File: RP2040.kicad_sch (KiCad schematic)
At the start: 28 parts, among them J3 USB_C_Receptacle_USB2.0_16P, U1 RP2040, U2 AMS1117-3.3, U4 W25Q16JVSS, Y1 X322512MSB4SI

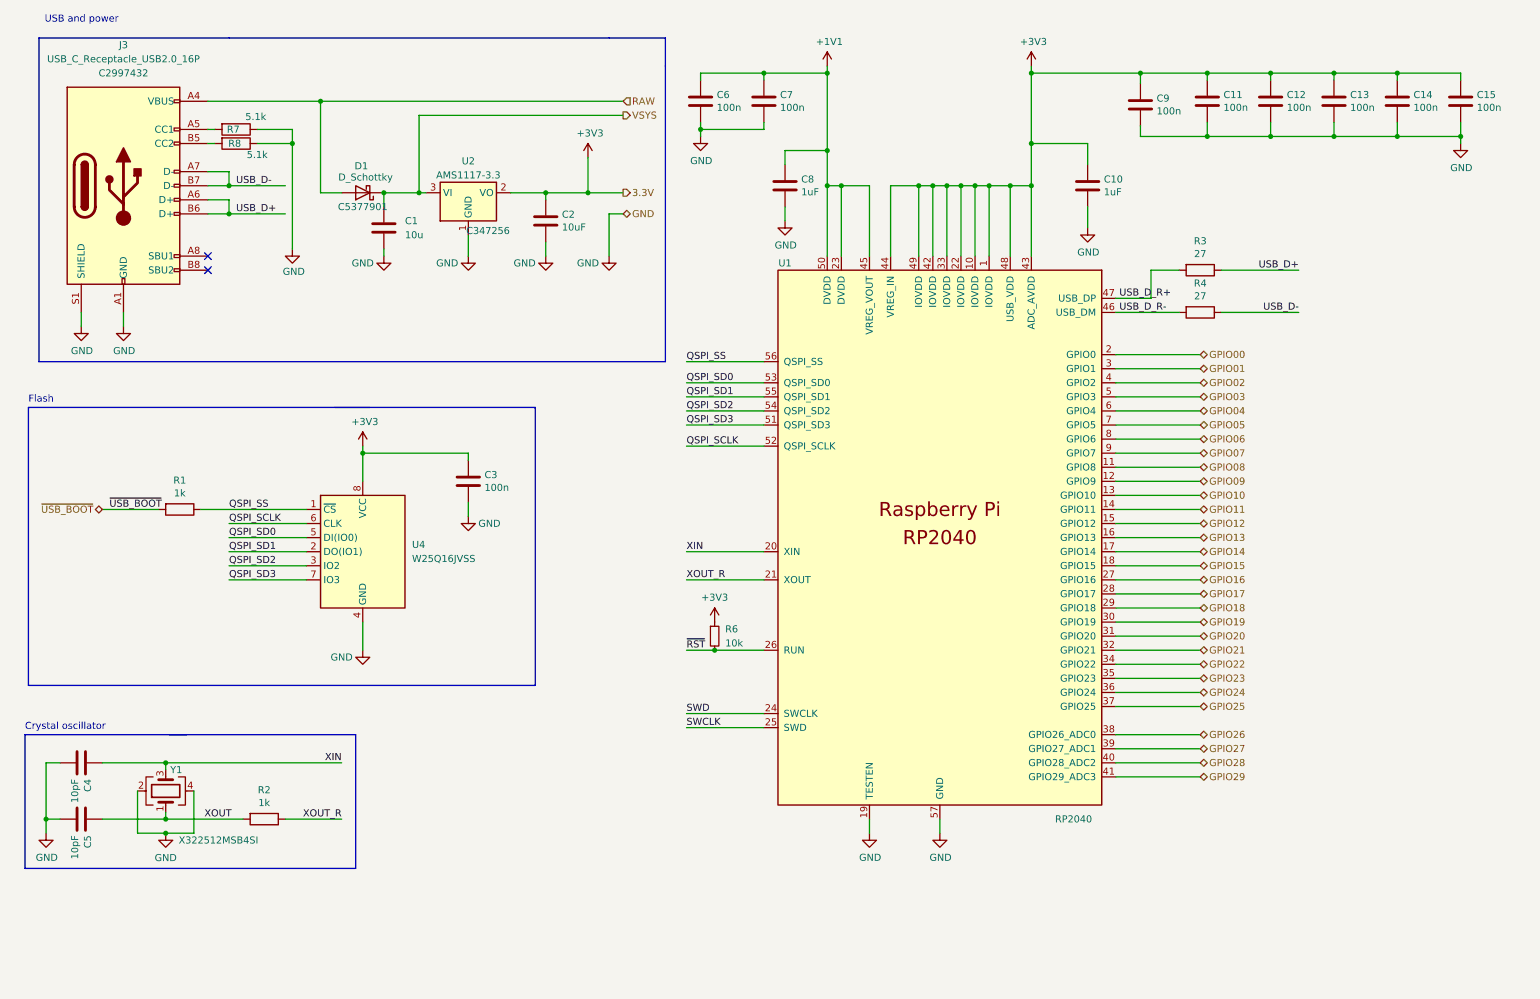
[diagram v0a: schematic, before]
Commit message: first changes for RP2350A
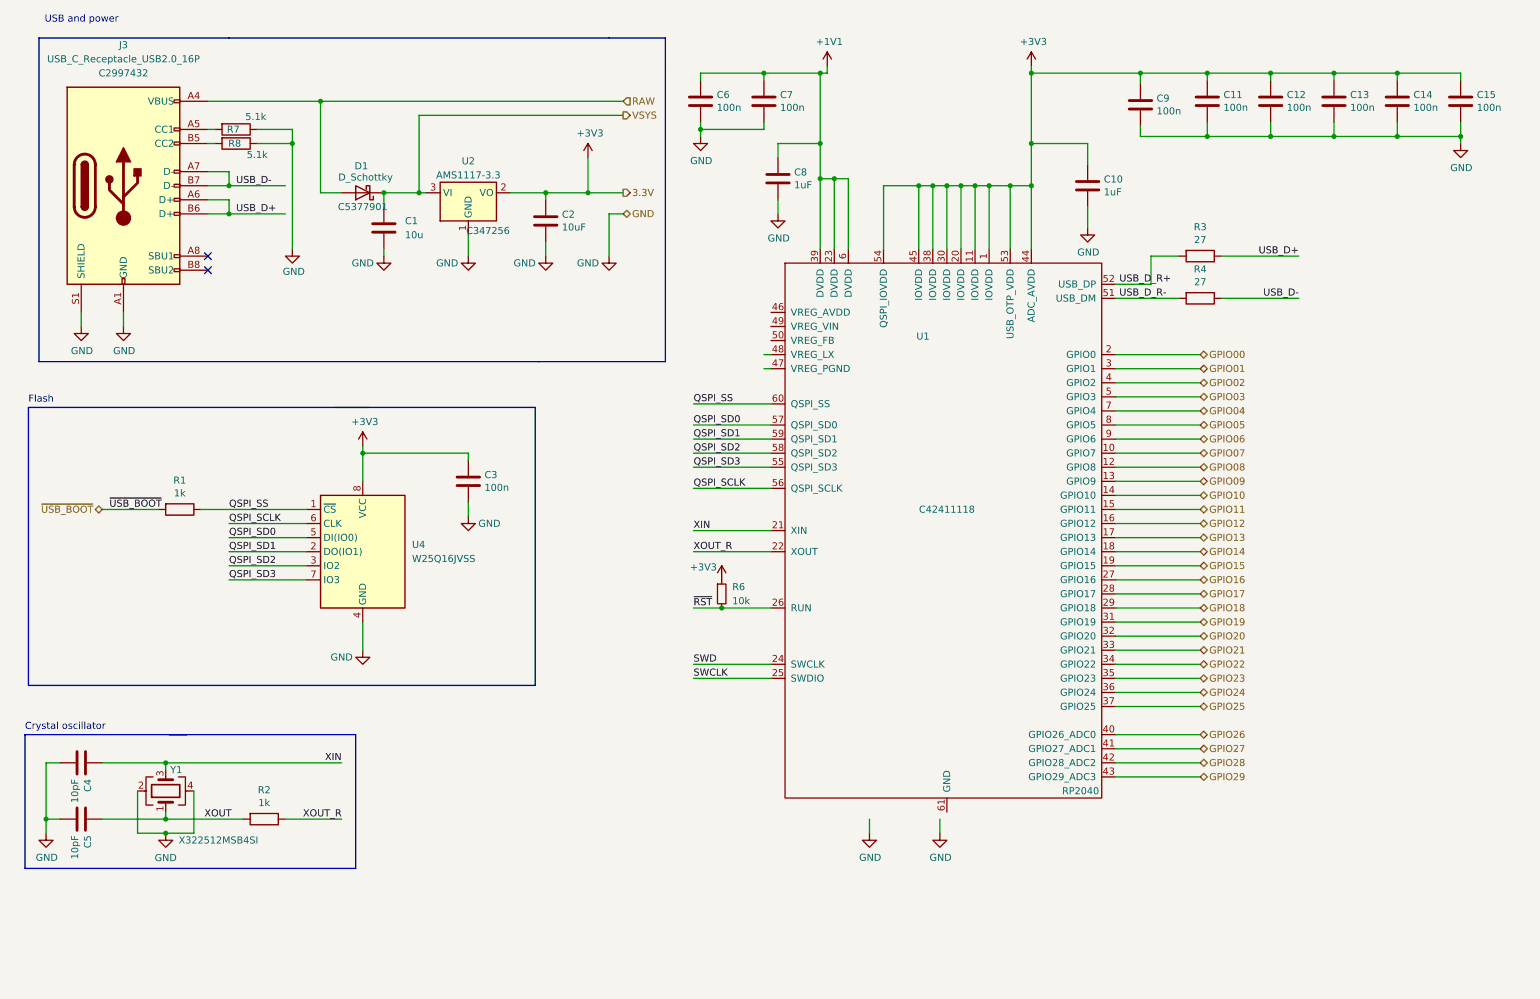
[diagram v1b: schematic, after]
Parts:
- U1: footprint _Neil:QFN56P40_700X700X90L40X18T310N -> _Own_Library:RP2350A_QFN-60_EP_7.75x7.75_Pitch0.4mm; symbol Custom_Symbols:RP2040 -> Own_Library:RP2350A-QFN60; JLCPCB (none) -> C42411118
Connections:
- net +1V1: now also U1.39 (DVDD), U1.6 (DVDD); no longer U1.45 (VREG_VOUT), U1.50 (DVDD)
- net +3V3: now also U1.11 (IOVDD), U1.20 (IOVDD), U1.30 (IOVDD), U1.38 (IOVDD), U1.45 (IOVDD), U1.53 (USB_OTP_VDD), U1.54 (QSPI_IOVDD); no longer U1.10 (IOVDD), U1.22 (IOVDD), U1.33 (IOVDD), U1.42 (IOVDD), U1.43 (ADC_AVDD), U1.48 (USB_VDD), U1.49 (IOVDD)
- net GND: no longer U1.19 (TESTEN), U1.57 (GND)
- net GPIO04: now also U1.7 (GPIO4); no longer U1.6 (GPIO4)
- net GPIO05: now also U1.8 (GPIO5); no longer U1.7 (GPIO5)
- net GPIO06: now also U1.9 (GPIO6); no longer U1.8 (GPIO6)
- net GPIO07: now also U1.10 (GPIO7); no longer U1.9 (GPIO7)
- net GPIO08: now also U1.12 (GPIO8); no longer U1.11 (GPIO8)
- net GPIO09: now also U1.13 (GPIO9); no longer U1.12 (GPIO9)
- net GPIO10: now also U1.14 (GPIO10); no longer U1.13 (GPIO10)
- net GPIO11: now also U1.15 (GPIO11); no longer U1.14 (GPIO11)
- net GPIO12: now also U1.16 (GPIO12); no longer U1.15 (GPIO12)
- net GPIO13: now also U1.17 (GPIO13); no longer U1.16 (GPIO13)
- net GPIO14: now also U1.18 (GPIO14); no longer U1.17 (GPIO14)
- net GPIO15: now also U1.19 (GPIO15); no longer U1.18 (GPIO15)
- net GPIO19: now also U1.31 (GPIO19); no longer U1.30 (GPIO19)
- net GPIO20: now also U1.32 (GPIO20); no longer U1.31 (GPIO20)
- net GPIO21: now also U1.33 (GPIO21); no longer U1.32 (GPIO21)
- net GPIO26: now also U1.40 (GPIO26_ADC0); no longer U1.38 (GPIO26_ADC0)
- net GPIO27: now also U1.41 (GPIO27_ADC1); no longer U1.39 (GPIO27_ADC1)
- net GPIO28: now also U1.42 (GPIO28_ADC2); no longer U1.40 (GPIO28_ADC2)
- net GPIO29: now also U1.43 (GPIO29_ADC3); no longer U1.41 (GPIO29_ADC3)
- net QSPI_SCLK: now also U1.56 (QSPI_SCLK); no longer U1.52 (QSPI_SCLK)
- net QSPI_SD0: now also U1.57 (QSPI_SD0); no longer U1.53 (QSPI_SD0)
- net QSPI_SD1: now also U1.59 (QSPI_SD1); no longer U1.55 (QSPI_SD1)
- net QSPI_SD2: now also U1.58 (QSPI_SD2); no longer U1.54 (QSPI_SD2)
- net QSPI_SD3: now also U1.55 (QSPI_SD3); no longer U1.51 (QSPI_SD3)
- net QSPI_SS: now also U1.60 (QSPI_SS); no longer U1.56 (QSPI_SS)
- net USB_D_R+: now also U1.52 (USB_DP); no longer U1.47 (USB_DP)
- net USB_D_R-: now also U1.51 (USB_DM); no longer U1.46 (USB_DM)
- net XIN: now also U1.21 (XIN); no longer U1.20 (XIN)
- net XOUT_R: now also U1.22 (XOUT); no longer U1.21 (XOUT)
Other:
- moved on the sheet: C8, R3, R4, R6

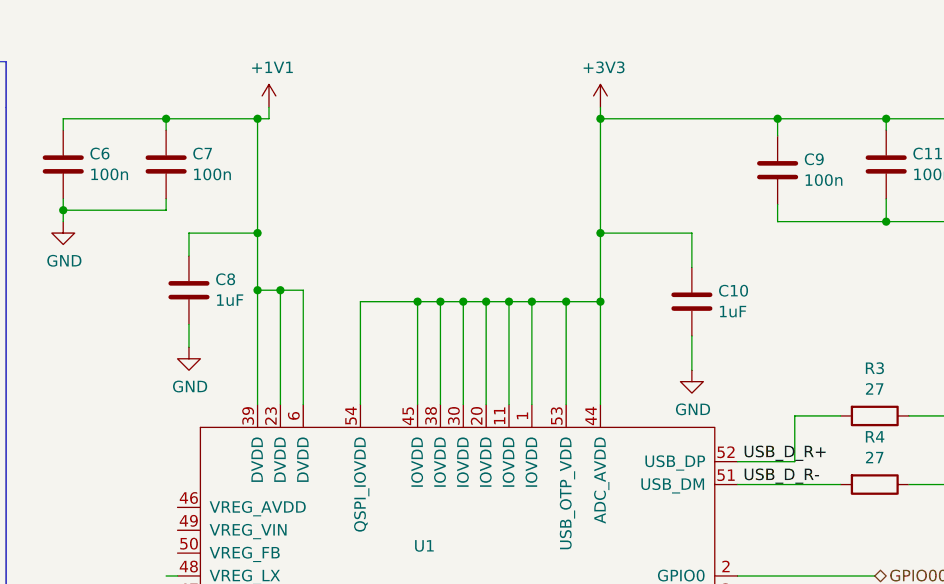
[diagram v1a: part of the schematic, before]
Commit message: power supply lines routed
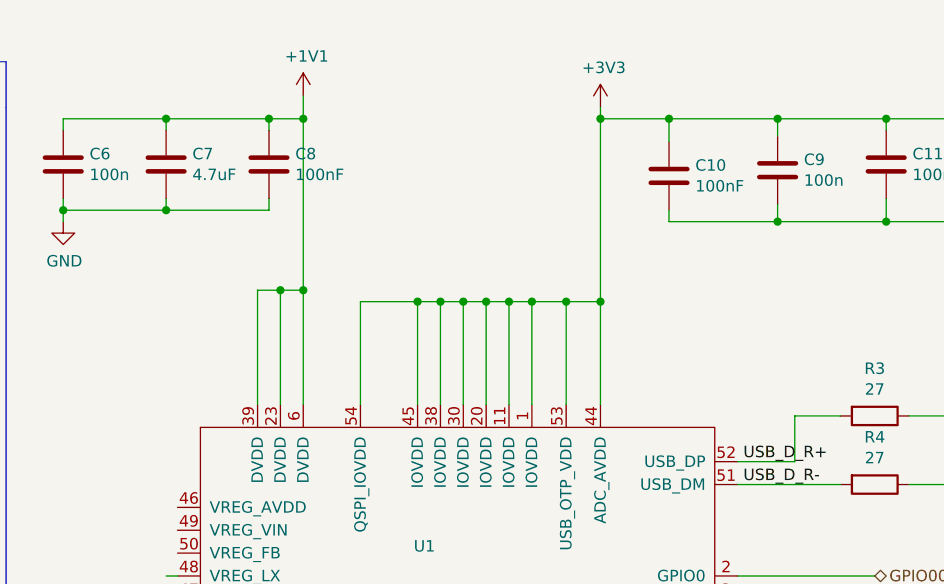
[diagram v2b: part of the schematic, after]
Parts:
- C10, C8: value 1uF -> 100nF
- C7: value 100n -> 4.7uF
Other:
- moved on the sheet: C10, C8

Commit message: fixed all warnings/errors
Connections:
- net GND: now also U1.61 (GND)
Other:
- moved on the sheet: C1, C10, C11, C12, C13, C14, C15, C2, C3, C4, C5, C6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

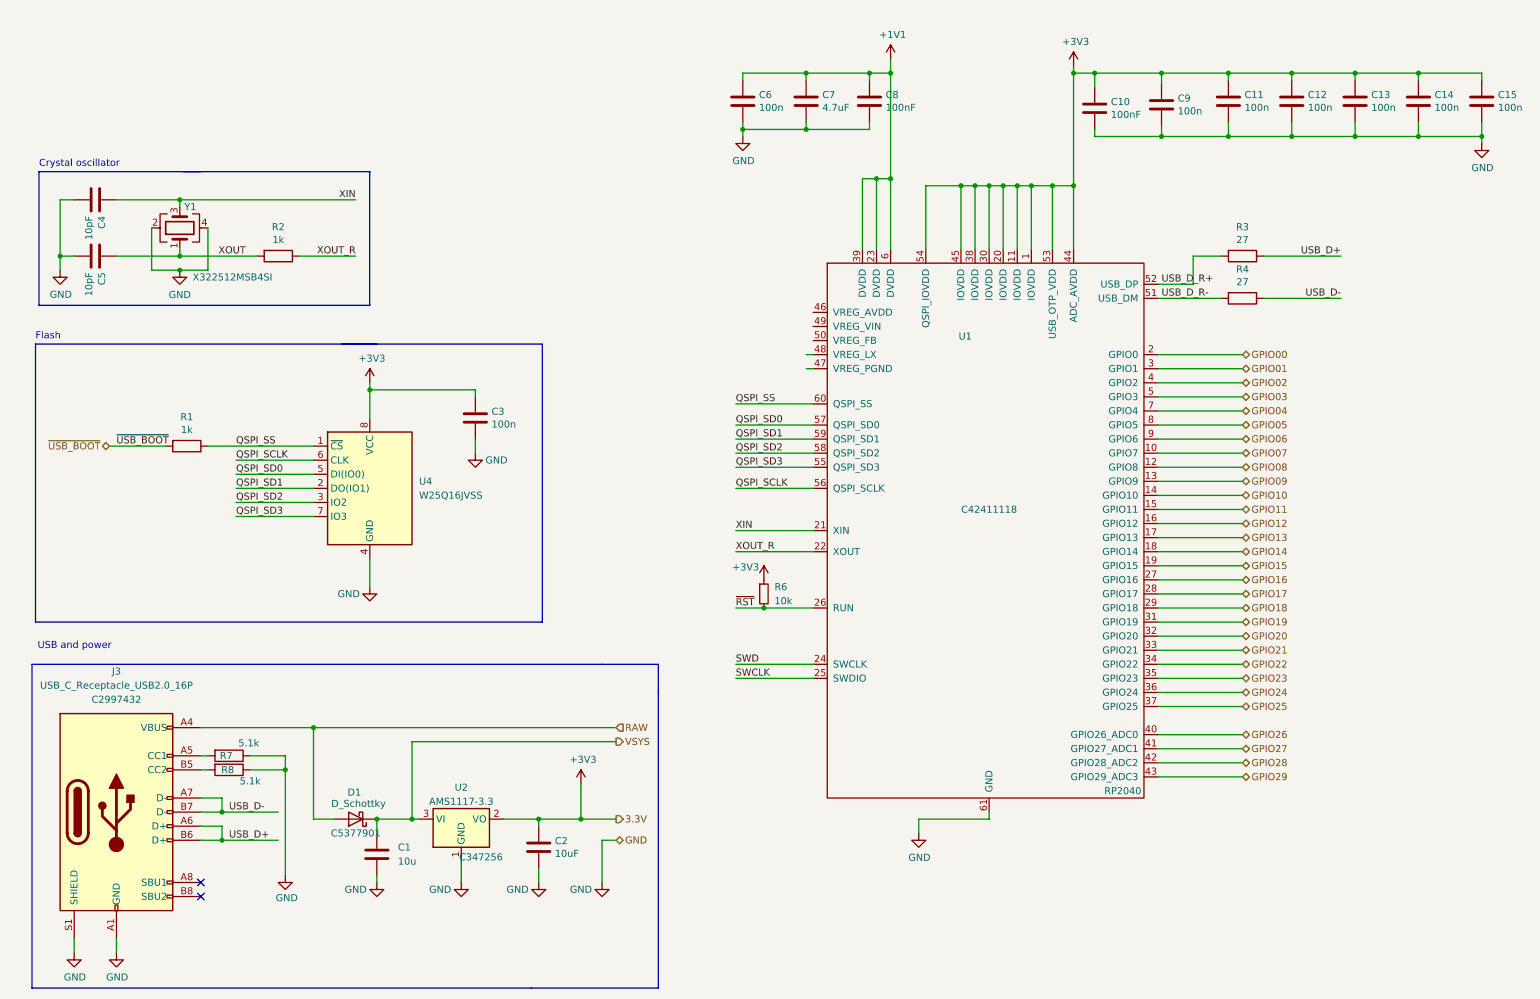
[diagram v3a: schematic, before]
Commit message: add parts for 1.1V regulator
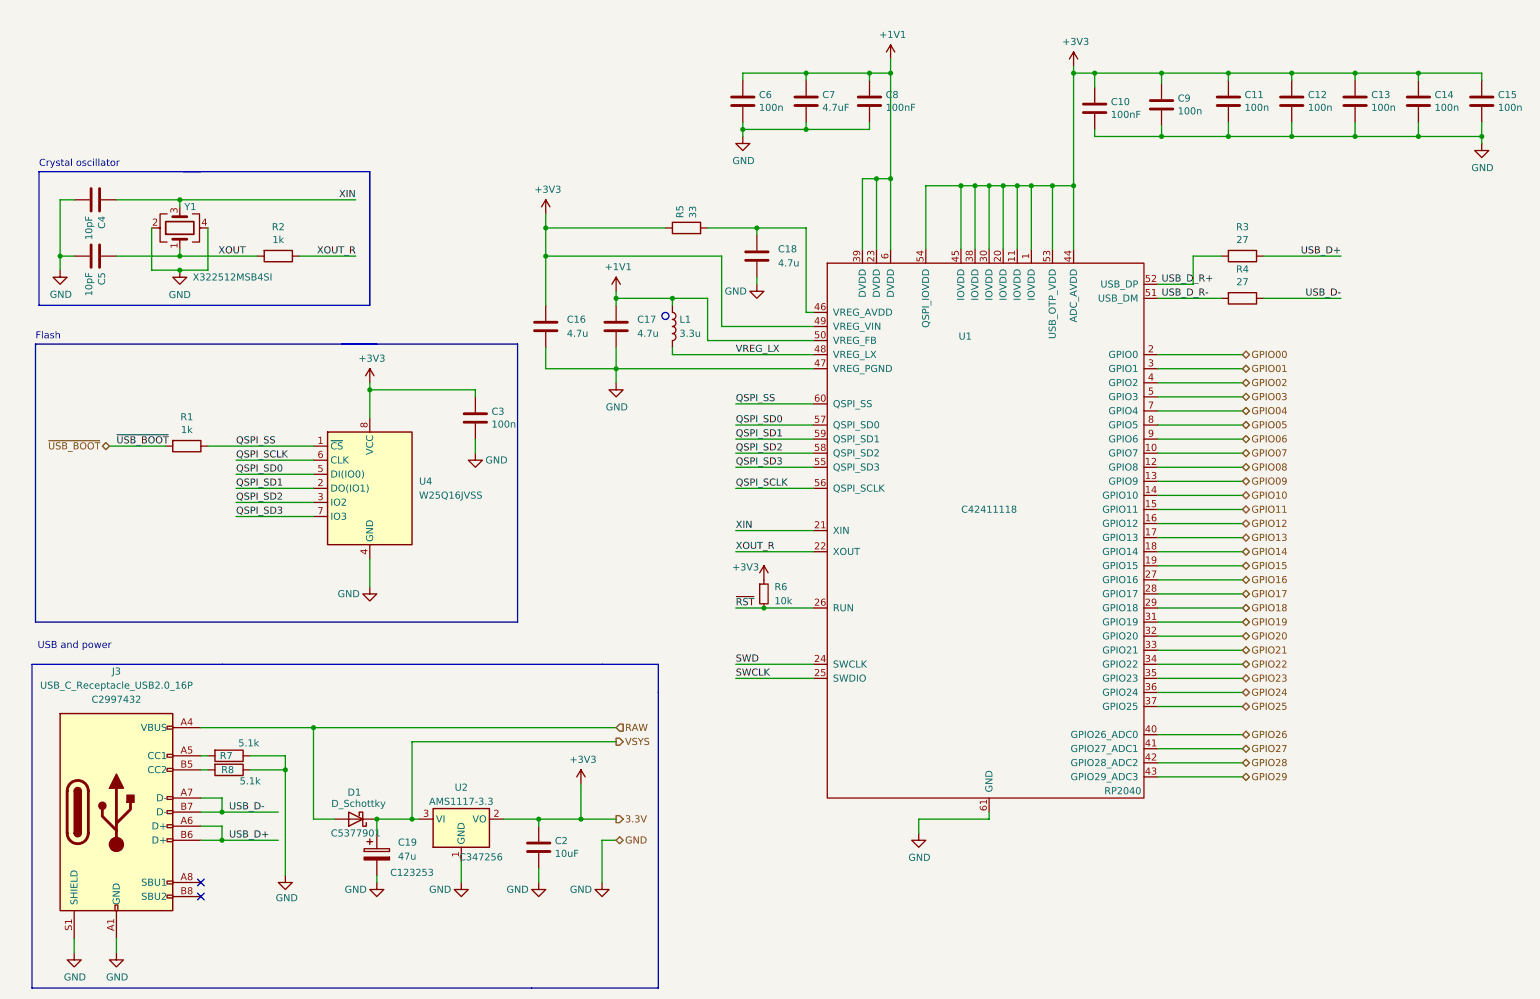
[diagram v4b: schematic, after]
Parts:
- removed C1: 10u, Capacitor_SMD:C_0402_1005Metric, symbol Device:C
- added C16, C17: 4.7u, _Own_Library:C_0402_1005Metric_small_pads, symbol Device:C
- added C18: 4.7u, Capacitor_SMD:C_0402_1005Metric, symbol Device:C
- added C19: 47u, Capacitor_Tantalum_SMD:CP_EIA-3528-21_Kemet-B, symbol Device:C_Polarized
- added L1: 3.3u, _Own_Library:L_pol_2016, symbol Device:L
- added R5: 33, Resistor_SMD:R_0402_1005Metric, symbol Device:R
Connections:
- net +1V1: now also U1.50 (VREG_FB), C17.1, L1.1
- net +3V3: now also U1.49 (VREG_VIN), C16.1, R5.1
- net GND: now also U1.47 (VREG_PGND), C16.2, C17.2, C18.2, C19.2
- net VSYS: now also C19.1
- net at U1.46 (VREG_AVDD): now also C18.1, R5.2
- net VREG_LX: now reaches U1.48 (VREG_LX)
- net VREG_LX: now also L1.2

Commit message: optimazations
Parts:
- removed C19: 47u, Capacitor_Tantalum_SMD:CP_EIA-3528-21_Kemet-B, symbol Device:C_Polarized
- added C1: 10uF, Capacitor_SMD:C_0402_1005Metric, symbol Device:C
- added SW1: SW_Push, Button_Switch_SMD:SW_Push_1P1T_NO_Vertical_Wuerth_434133025816, symbol Switch:SW_Push
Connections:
- net GND: now also C1.2, SW1.1
- net VSYS: now also C1.1
- net ~{USB_BOOT}: now also SW1.2
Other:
- note removed: "Crystal oscillator"
- moved on the sheet: C3, C4, C5, R1, R2, U4, Y1
